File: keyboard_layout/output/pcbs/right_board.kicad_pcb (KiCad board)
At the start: 2 copper layers, 142.5 x 113 mm, 66 parts

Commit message: Update pcb size
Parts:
- removed the ? at (96.0, 10.8)
- removed the ? at (11.5, 3.81)
- removed the ? at (11.5, -55.2)
- removed the ? at (97.1, -48.2)
- removed the ? at (48.9, -36.5)
- added ?: , HOLE_M2_TH, F.Cu at (183.5, 26.2)
- added ?: , HOLE_M2_TH, F.Cu at (284.2, 11.5)
- added ?: , HOLE_M2_TH, F.Cu at (284.2, -68.5)
- added ?: , HOLE_M2_TH, F.Cu at (166.9, -60.6)
- added ?: , HOLE_M2_TH, F.Cu at (236.7, -37.9)
- moved D1 286.3 mm to (294.2, 3.50)
- moved D2 286.3 mm to (294.2, -15.5)
- moved D3 286.3 mm to (294.2, -34.5)
- moved D4 286.3 mm to (294.2, -53.5)
- moved S1 286.2 mm to (286.2, 0.00)
- moved S2 286.2 mm to (286.2, -19.0)
- moved S3 286.2 mm to (286.2, -38.0)
- moved S4 286.2 mm to (286.2, -57.0)
- moved D5 248.3 mm to (275.2, -2.21)
- moved D6 248.3 mm to (275.2, -21.2)
- moved D7 248.3 mm to (275.2, -40.2)
- moved D8 248.3 mm to (275.2, -59.2)
- moved S5 248.2 mm to (267.2, -5.71)
- moved S6 248.2 mm to (267.2, -24.7)
- moved S7 248.2 mm to (267.2, -43.7)
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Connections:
- net curly_square renamed mirror_curly_square
- net far_thumb renamed mirror_far_thumb
- net five_bottom renamed mirror_five_bottom
- net five_home renamed mirror_five_home
- net five_number renamed mirror_five_number
- net five_qwerty renamed mirror_five_qwerty
- net four_bottom renamed mirror_four_bottom
- net four_home renamed mirror_four_home
- net four_number renamed mirror_four_number
- net four_qwerty renamed mirror_four_qwerty
- net function_keys_bottom renamed mirror_function_keys_bottom
- net function_keys_home renamed mirror_function_keys_home
- net function_keys_number renamed mirror_function_keys_number
- net function_keys_qwerty renamed mirror_function_keys_qwerty
- net home_thumb renamed mirror_home_thumb
- net near_thumb renamed mirror_near_thumb
- net one_bottom renamed mirror_one_bottom
- net one_home renamed mirror_one_home
- net one_number renamed mirror_one_number
- net one_qwerty renamed mirror_one_qwerty
- net space_thumb renamed mirror_space_thumb
- net three_bottom renamed mirror_three_bottom
- net three_home renamed mirror_three_home
- net three_number renamed mirror_three_number
- net three_qwerty renamed mirror_three_qwerty
- net two_bottom renamed mirror_two_bottom
- net two_home renamed mirror_two_home
- net two_number renamed mirror_two_number
- net two_qwerty renamed mirror_two_qwerty
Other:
- board size 142.5 x 113 mm -> 144.1 x 115 mm

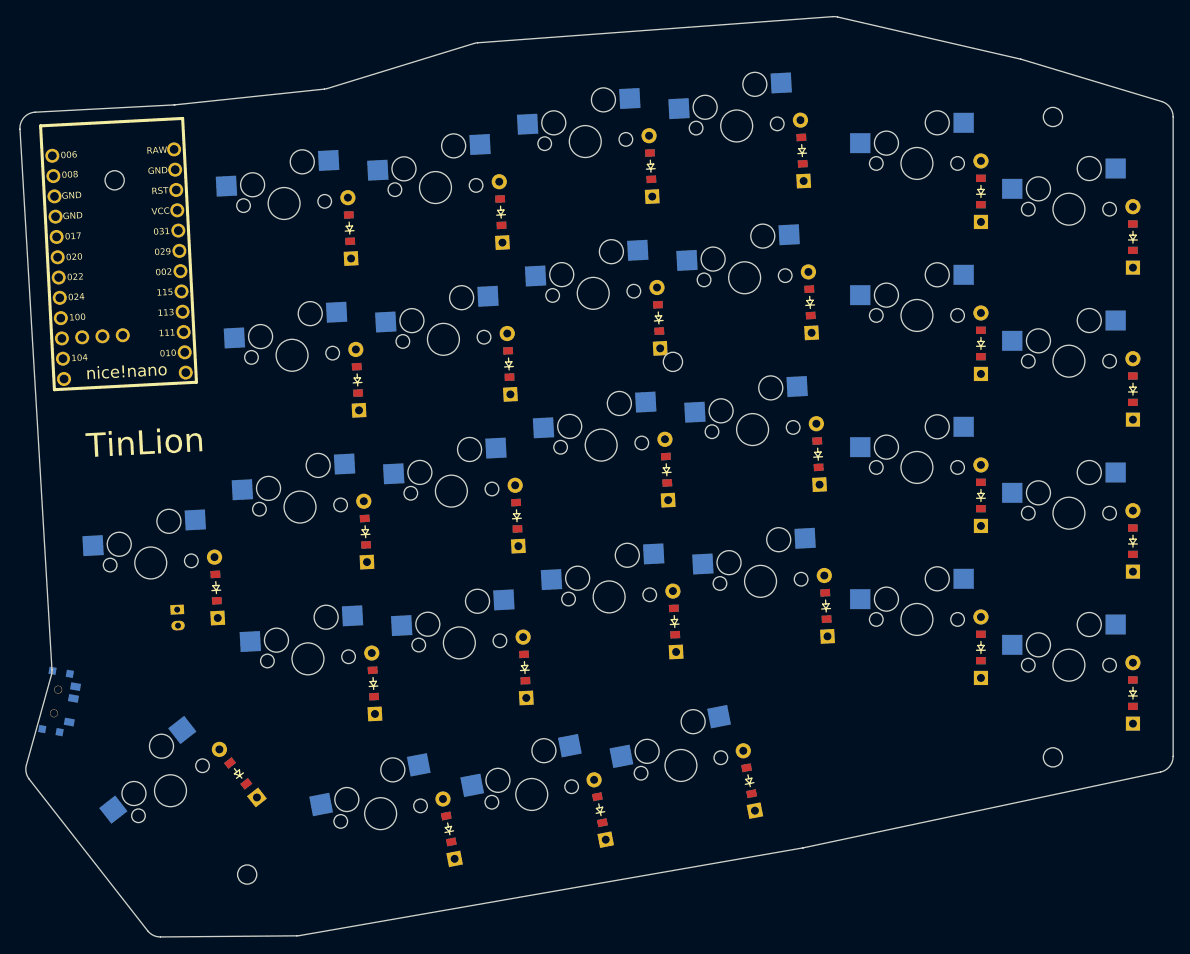
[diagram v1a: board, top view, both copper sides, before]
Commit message: Move mount screw holes
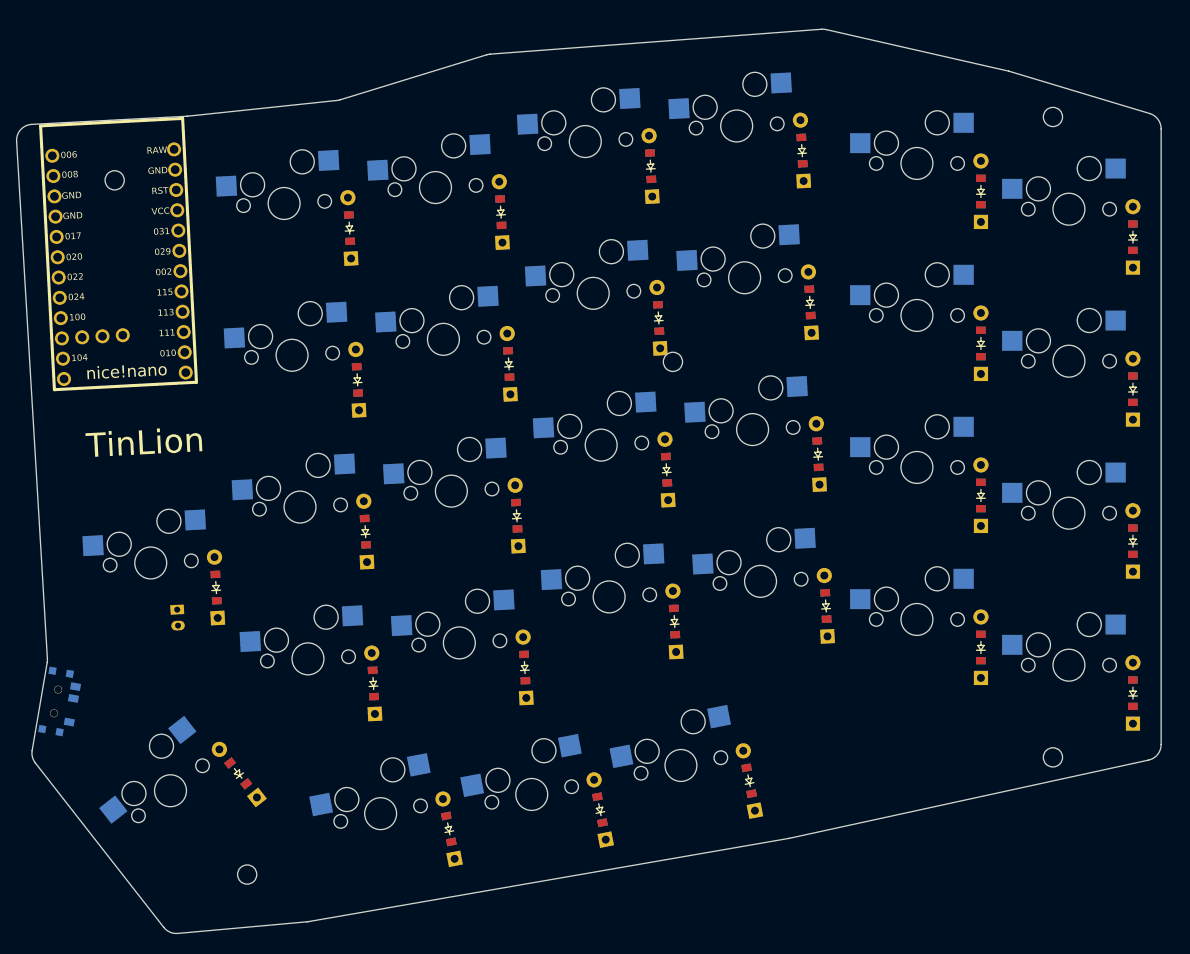
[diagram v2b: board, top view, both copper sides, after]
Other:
- board size 144.1 x 115 mm -> 143.1 x 113 mm
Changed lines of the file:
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@@
                 (effects (font (size 3 3) (thickness 0.4) ) (justify left))
             )
-  (gr_line (start 299.2321942 11.40478424410076) (end 299.2321942 -68.5380634051579) (angle 90) (layer Edge.Cuts) (width 0.15))
-(gr_line (start 297.80827697241665 -70.45329931345465) (end 280.29534388377607 -75.7210052398537) (angle 90) (layer Edge.Cuts) (width 0.15))
-(gr_line (start 280.16793048949773 -75.75479363658953) (end 257.2938457341869 -81.02045437331323) (angle 90) (layer Edge.Cuts) (width 0.15))
-(gr_line (start 256.6983089555094 -81.06603027560416) (end 212.28590422860242 -77.79583202507769) (angle 90) (layer Edge.Cuts) (width 0.15))
-(gr_line (start 211.84563466582327 -77.71310789830908) (end 193.52148203593595 -72.08576305145404) (angle 90) (layer Edge.Cuts) (width 0.15))
-(gr_line (start 193.14384588303494 -72.00864203310621) (end 174.46707772542328 -70.04142009843459) (angle 90) (layer Edge.Cuts) (width 0.15))
-(gr_line (start 174.36224891995838 -70.03315810283766) (end 156.97730945122356 -69.12205198617649) (angle 90) (layer Edge.Cuts) (width 0.15))
-(gr_line (start 155.0854780561761 -67.00658049167669) (end 159.0872382819993 0.5796557503786062) (angle 90) (layer Edge.Cuts) (width 0.15))
-(gr_line (start 159.01762440063328 1.2336823833671815) (end 155.89010945155246 12.480817359715388) (angle 90) (layer Edge.Cuts) (width 0.15))
-(gr_line (start 156.24097743228245 14.247954544189469) (end 171.05098265994974 33.203896698935154) (angle 90) (layer Edge.Cuts) (width 0.15))
-(gr_line (start 172.64336259867818 33.97250684826114) (end 189.70345988719325 33.83296342610927) (angle 90) (layer Edge.Cuts) (width 0.15))
-(gr_line (start 190.03033928636864 33.80335712529806) (end 252.94381186495124 22.84361245495728) (angle 90) (layer Edge.Cuts) (width 0.15))
-(gr_line (start 253.01563228955916 22.82974337095157) (end 297.6472524246079 13.361241960095029) (angle 90) (layer Edge.Cuts) (width 0.15))
-(gr_arc (start 297.2321942 -68.5380634051579) (end 299.2321942 -68.5380634051579) (angle -73.25926693492208) (layer Edge.Cuts) (width 0.15))
-(gr_arc (start 279.71926111135946 -73.80576933155689) (end 280.29534391135945 -75.72100523155689) (angle -3.7769744047999723) (layer Edge.Cuts) (width 0.15))
-(gr_arc (start 256.8451763560486 -79.07143006828059) (end 257.29384575604865 -81.0204543682806) (angle -17.174990398252817) (layer Edge.Cuts) (width 0.15))
-(gr_arc (start 212.43277162914166 -75.80123181775414) (end 212.28590422914166 -77.79583201775414) (angle -12.86048545222124) (layer Edge.Cuts) (width 0.15))
-(gr_arc (start 192.93434507261753 -73.99763913200897) (end 193.14384587261753 -72.00864203200896) (angle -11.058930695448964) (layer Edge.Cuts) (width 0.15))
-(gr_arc (start 174.25757691500584 -72.03041719733733) (end 174.36224891500584 -70.03315809733733) (angle -3.0127838868756953) (layer Edge.Cuts) (width 0.15))
-(gr_arc (start 157.08198145617607 -67.12479289167683) (end 156.97730945617607 -69.12205199167683) (angle -90.38850813719506) (layer Edge.Cuts) (width 0.15))
-(gr_arc (start 157.09073488199928 0.6978681503783264) (end 159.01762438199927 1.2336823503783263) (angle -18.928276491824104) (layer Edge.Cuts) (width 0.15))
-(gr_arc (start 157.81699897018638 13.016631592704243) (end 155.8901094701864 12.480817392704243) (angle -53.53976522429252) (layer Edge.Cuts) (width 0.15))
-(gr_arc (start 172.62700419785364 31.97257374744993) (end 171.05098269785364 33.20389664744993) (angle -52.468639410966034) (layer Edge.Cuts) (width 0.15))
-(gr_arc (start 189.68710148636868 31.83303032529807) (end 189.70345988636868 33.83296342529807) (angle -9.413319927294424) (layer Edge.Cuts) (width 0.15))
-(gr_arc (start 252.60057406495125 20.873285654957293) (end 252.94381186495124 22.84361245495729) (angle -2.0956320832463007) (layer Edge.Cuts) (width 0.15))
-(gr_arc (start 297.2321942 11.40478424410076) (end 297.64725239999996 13.36124194410076) (angle -78.02240910096532) (layer Edge.Cuts) (width 0.15))
+  (gr_line (start 297.7321942 9.91357778409214) (end 297.7321942 -67.0380634051579) (angle 90) (layer Edge.Cuts) (width 0.15))
+(gr_line (start 296.3082769724166 -68.95329931345469) (end 278.7976217262919 -74.22032008880221) (angle 90) (layer Edge.Cuts) (width 0.15))
+(gr_line (start 278.66557535387517 -74.25516918050545) (end 255.87369931368096 -79.4449030444585) (angle 90) (layer Edge.Cuts) (width 0.15))
+(gr_line (start 255.27978830620827 -79.48919454389697) (end 213.86080468204776 -76.37661611728166) (angle 90) (layer Edge.Cuts) (width 0.15))
+(gr_line (start 213.42354232620195 -76.29411569839813) (end 195.09793023593605 -70.66632265145407) (angle 90) (layer Edge.Cuts) (width 0.15))
+(gr_line (start 194.72029408303504 -70.58920163310623) (end 176.04352592607776 -68.62197969850351) (angle 90) (layer Edge.Cuts) (width 0.15))
+(gr_line (start 175.93869712061283 -68.61371770290658) (end 156.55710875863195 -67.59797165922595) (angle 90) (layer Edge.Cuts) (width 0.15))
+(gr_line (start 154.66531336358443 -65.48189456472664) (end 158.5154698618605 -0.7887567923867209) (angle 90) (layer Edge.Cuts) (width 0.15))
+(gr_line (start 158.4903714618604 -0.3327379923866829) (end 156.61105961599628 10.654237968498137) (angle 90) (layer Edge.Cuts) (width 0.15))
+(gr_line (start 157.0064070780924 12.222761719983339) (end 173.06083624315625 32.77149393312959) (angle 90) (layer Edge.Cuts) (width 0.15))
+(gr_line (start 174.81585558025915 33.53214477273045) (end 190.97273229830432 32.080296120431214) (angle 90) (layer Edge.Cuts) (width 0.15))
+(gr_line (start 191.13508329910533 32.058977329345176) (end 251.17896505745406 21.658422222747845) (angle 90) (layer Edge.Cuts) (width 0.15))
+(gr_line (start 251.2630780619795 21.641988843534016) (end 296.15765600452534 11.86779940487834) (angle 90) (layer Edge.Cuts) (width 0.15))
+(gr_arc (start 295.7321942 -67.0380634051579) (end 297.7321942 -67.0380634051579) (angle -73.25926693492399) (layer Edge.Cuts) (width 0.15))
+(gr_arc (start 278.2215389538752 -72.30508418050543) (end 278.7976217538752 -74.22032008050543) (angle -3.913133492553399) (layer Edge.Cuts) (width 0.15))
+(gr_arc (start 255.42966291368091 -77.49481804445851) (end 255.8736993136809 -79.44490304445851) (angle -17.1252194979552) (layer Edge.Cuts) (width 0.15))
+(gr_arc (start 214.01067928952037 -74.38223961784321) (end 213.86080468952036 -76.37661611784321) (angle -12.774097264771527) (layer Edge.Cuts) (width 0.15))
+(gr_arc (start 194.5107932726176 -72.57819873200897) (end 194.7202940726176 -70.58920163200897) (angle -11.058930695449021) (layer Edge.Cuts) (width 0.15))
+(gr_arc (start 175.83402511566032 -70.61097679740625) (end 175.93869711566032 -68.61371769740626) (angle -3.012783886876548) (layer Edge.Cuts) (width 0.15))
+(gr_arc (start 156.66178076358446 -65.6007125647263) (end 156.55710876358447 -67.59797166472629) (angle -90.40588792603558) (layer Edge.Cuts) (width 0.15))
+(gr_arc (start 156.51900246186048 -0.6699387923868017) (end 158.4903714618605 -0.33273799238680163) (angle -13.11234371841013) (layer Edge.Cuts) (width 0.15))
+(gr_arc (start 158.5824286159963 10.991438768498142) (end 156.61105961599628 10.654237968498142) (angle -47.70645266201359) (layer Edge.Cuts) (width 0.15))
+(gr_arc (start 174.63685778106017 31.540170981644394) (end 173.06083628106018 32.771493881644396) (angle -57.134780469852814) (layer Edge.Cuts) (width 0.15))
+(gr_arc (start 190.79373449910534 30.088322329345182) (end 190.97273229910533 32.08029612934518) (angle -4.692252290154499) (layer Edge.Cuts) (width 0.15))
+(gr_arc (start 250.83761625745407 19.687767222747844) (end 251.17896505745406 21.658422222747845) (angle -2.4554062176344473) (layer Edge.Cuts) (width 0.15))
+(gr_arc (start 295.7321942 9.91357778409214) (end 296.157656 11.867799384092141) (angle -77.71756154483643) (layer Edge.Cuts) (width 0.15))
 )

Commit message: gerberfiles added, leftright pcbs
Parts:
- removed the ? at (183.5, 26.2)
- removed the ? at (284.2, 11.5)
- removed the ? at (284.2, -68.5)
- removed the ? at (166.9, -60.6)
- removed the ? at (236.7, -37.9)
- added ?: , HOLE_M2_TH, F.Cu at (376.5, 176.0)
- added ?: , HOLE_M2_TH, F.Cu at (376.5, 96.0)
- added ?: , HOLE_M2_TH, F.Cu at (275.7, 190.7)
- added ?: , HOLE_M2_TH, F.Cu at (329.0, 126.6)
- added ?: , HOLE_M2_TH, F.Cu at (259.2, 103.9)
- moved S22 188.6 mm to (282.3, 144.7)
- moved D21 188.6 mm to (291.5, 166.8)
- moved S19 188.6 mm to (300.3, 123.8)
- moved S11 188.6 mm to (337.9, 116.1)
- moved S14 188.6 mm to (320.0, 137.0)
- moved D18 188.6 mm to (309.4, 145.8)
- moved D26 188.6 mm to (319.8, 182.6)
- moved D13 188.6 mm to (329.2, 159.0)
- moved D16 188.6 mm to (326.2, 102.1)
- moved S21 188.6 mm to (283.3, 163.7)
- moved D27 188.6 mm to (300.9, 185.0)
- moved S25 188.6 mm to (330.0, 177.0)
- moved S18 188.6 mm to (301.3, 142.7)
- moved S10 188.6 mm to (338.9, 135.0)
- moved D17 188.6 mm to (310.4, 164.8)
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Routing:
- net P006: track 0.00 -> 199.1 mm
- net P111: track 0.00 -> 193.2 mm
- net P113: track 0.00 -> 189.2 mm
- net P031: track 0.00 -> 167.5 mm
- net P008: track 0.00 -> 156.9 mm
- net P010: track 0.00 -> 154.6 mm
- net P115: track 0.00 -> 152.8 mm
- net P002: track 0.00 -> 147.9 mm
- net P029: track 0.00 -> 144.6 mm
- net P017: track 0.00 -> 140.7 mm
- net P020: track 0.00 -> 102.3 mm
- net GND: track 0.00 -> 88.8 mm
- net RAW: track 0.00 -> 85.9 mm
- net P104: track 0.00 -> 57.5 mm
- net pos: track 0.00 -> 19.7 mm, vias 0 -> 1
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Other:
- net class Default removed

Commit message: Update final keyboard pcb
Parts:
- removed the ? at (376.5, 176.0)
- removed the ? at (376.5, 96.0)
- removed the ? at (275.7, 190.7)
- removed the ? at (329.0, 126.6)
- removed the ? at (259.2, 103.9)
- added ?: , HOLE_M2_TH, F.Cu at (183.5, 26.2)
- added ?: , HOLE_M2_TH, F.Cu at (284.2, 9.53)
- added ?: , HOLE_M2_TH, F.Cu at (279.2, -68.5)
- added ?: , HOLE_M2_TH, F.Cu at (187.6, -66.7)
- added ?: , HOLE_M2_TH, F.Cu at (208.5, -31.0)
- added ?: , HOLE_M2_TH, F.Cu at (255.8, -37.4)
- moved S22 188.6 mm to (190.1, -19.8)
- moved D21 188.6 mm to (199.3, 2.29)
- moved S19 188.6 mm to (208.0, -40.7)
- moved S11 188.6 mm to (245.7, -48.4)
- moved S14 188.6 mm to (227.7, -27.5)
- moved D18 188.6 mm to (217.2, -18.7)
- moved D26 188.6 mm to (227.6, 18.1)
- moved D13 188.6 mm to (236.9, -5.46)
- moved D16 188.6 mm to (233.9, -62.4)
- moved S21 188.6 mm to (191.1, -0.79)
- moved D27 188.6 mm to (208.7, 20.5)
- moved S25 188.6 mm to (237.7, 12.5)
- moved S18 188.6 mm to (209.0, -21.8)
- moved S10 188.6 mm to (246.7, -29.5)
- moved D17 188.6 mm to (218.2, 0.29)
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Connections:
- D1 pad 1: P111 -> P115
- D10 pad 1: P113 -> P002
- D11 pad 1: P115 -> P029
- D12 pad 1: P002 -> P031
- D13 pad 1: P111 -> P115
- D14 pad 1: P113 -> P002
- D15 pad 1: P115 -> P029
- D16 pad 1: P002 -> P031
- D17 pad 1: P111 -> P115
- D18 pad 1: P113 -> P002
- D19 pad 1: P115 -> P029
- D2 pad 1: P113 -> P002
- D20 pad 1: P002 -> P031
- D21 pad 1: P111 -> P115
- D22 pad 1: P113 -> P002
- D23 pad 1: P115 -> P029
- D24 pad 1: P002 -> P031
- D25 pad 1: P010 -> P113
- D26 pad 1: P010 -> P113
- D27 pad 1: P010 -> P113
- D28 pad 1: P010 -> P113
- D29 pad 1: P113 -> P002
- D3 pad 1: P115 -> P029
- D4 pad 1: P002 -> P031
- D5 pad 1: P111 -> P115
- D6 pad 1: P113 -> P002
- D7 pad 1: P115 -> P029
- D8 pad 1: P002 -> P031
- D9 pad 1: P111 -> P115
- S1 pad 1: P006 -> P020
- S10 pad 1: P008 -> P024
- S11 pad 1: P008 -> P024
- S12 pad 1: P008 -> P024
- S13 pad 1: P029 -> P100
- S14 pad 1: P029 -> P100
- S15 pad 1: P029 -> P100
- S16 pad 1: P029 -> P100
- S17 pad 1: P017 -> P011
- S18 pad 1: P017 -> P011
- S19 pad 1: P017 -> P011
- S2 pad 1: P006 -> P020
- S20 pad 1: P017 -> P011
- S21 pad 1: P020 -> P104
- S22 pad 1: P020 -> P104
- S23 pad 1: P020 -> P104
- S24 pad 1: P020 -> P104
- S25 pad 1: P029 -> P100
- S26 pad 1: P017 -> P011
- S27 pad 1: P020 -> P104
- S28 pad 1: P104 -> P017
- S29 pad 1: P104 -> P017
- S3 pad 1: P006 -> P020
- S4 pad 1: P006 -> P020
- S5 pad 1: P031 -> P022
- S6 pad 1: P031 -> P022
- S7 pad 1: P031 -> P022
- S8 pad 1: P031 -> P022
- S9 pad 1: P008 -> P024
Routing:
- net P006: track 199.1 -> 0.00 mm
- net P111: track 193.2 -> 0.00 mm
- net P113: track 189.2 -> 0.00 mm
- net P031: track 167.5 -> 0.00 mm
- net P008: track 156.9 -> 0.00 mm
- net P010: track 154.6 -> 0.00 mm
- net P115: track 152.8 -> 0.00 mm
- net P002: track 147.9 -> 0.00 mm
- net P029: track 144.6 -> 0.00 mm
- net P017: track 140.7 -> 0.00 mm
- net P020: track 102.3 -> 0.00 mm
- net GND: track 88.8 -> 0.00 mm
- net RAW: track 85.9 -> 0.00 mm
- net P104: track 57.5 -> 0.00 mm
- net pos: track 19.7 -> 0.00 mm, vias 1 -> 0
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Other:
- net class Default added: clearance 0.2, trace_width 0.25, via_dia 0.8, via_drill 0.4
- board text added: "TINLION"
- board text removed: "TinLion"
